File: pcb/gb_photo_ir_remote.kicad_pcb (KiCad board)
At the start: 2 copper layers, 28 x 41 mm, 10 parts, among them SW1 SW_Push_SPDT, SW2 SW_Push_SPDT, U1 NE555P

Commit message: build
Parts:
- added M1: MountingHole_2.5mm, MountingHole:MountingHole_2.5mm, F.Cu at (123.0, 31.0)
- added M2: MountingHole_2.5mm, MountingHole:MountingHole_2.5mm, F.Cu at (152.0, 31.0)
- added M3: MountingHole_2.5mm, MountingHole:MountingHole_2.5mm, F.Cu at (123.0, 80.0)
- BT1: footprint Battery:BatteryHolder_Keystone_1060_1x2032 -> REB:REB_BatteryHolder_2032
- C1: footprint Capacitor_THT:C_Disc_D5.1mm_W3.2mm_P5.00mm -> Capacitor_THT:C_Disc_D5.0mm_W2.5mm_P2.50mm
- D1, D2: footprint LED_THT:LED_D5.0mm_Horizontal_O3.81mm_Z3.0mm -> LED_THT:LED_D5.0mm_Horizontal_O1.27mm_Z3.0mm
- moved U1 41.8 mm to (128.5, 79.8), turned to 90 degrees
- moved C1 40.1 mm to (146.8, 77.8), turned to 45 degrees
- moved R2 19.2 mm to (147.6, 70.3), turned to -135 degrees
- moved R1 18.0 mm to (150.7, 37.6), turned to 180 degrees
- moved R3 8.30 mm to (135.8, 37.6), turned to 180 degrees
- moved SW2 8.23 mm to (124.2, 63.1)
- moved SW1 7.20 mm to (144.7, 62.2)
- moved D1 5.98 mm to (144.3, 33.0)
- moved D2 4.45 mm to (134.2, 33.1)
- moved BT1 1.24 mm to (136.8, 50.7), turned to 0 degrees
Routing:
- net /OUT: track 0.00 -> 51.1 mm
- net Net-(D2-A): track 0.00 -> 49.4 mm
- net +BATT: track 0.00 -> 39.9 mm
- net /VIN: track 0.00 -> 39.7 mm
- net /DIS: track 0.00 -> 25.7 mm
- net Net-(D1-K): track 0.00 -> 9.38 mm
- net Net-(D2-K): track 0.00 -> 5.16 mm
- net GND: vias 0 -> 16
- added copper zone on B.Cu, net GND
- added copper zone on F.Cu, net GND
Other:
- board size 28 x 41 mm -> 35 x 55 mm

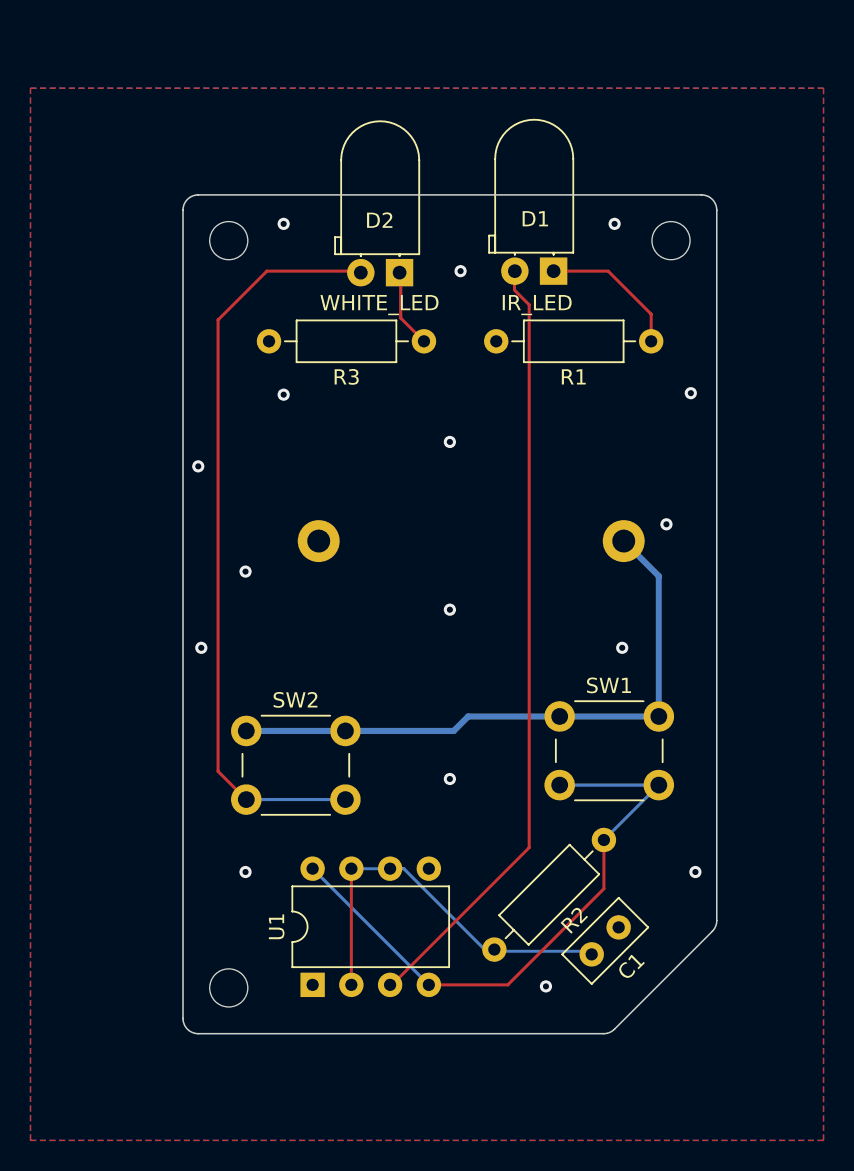
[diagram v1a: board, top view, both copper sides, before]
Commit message: Timer didn't use an actual divider?
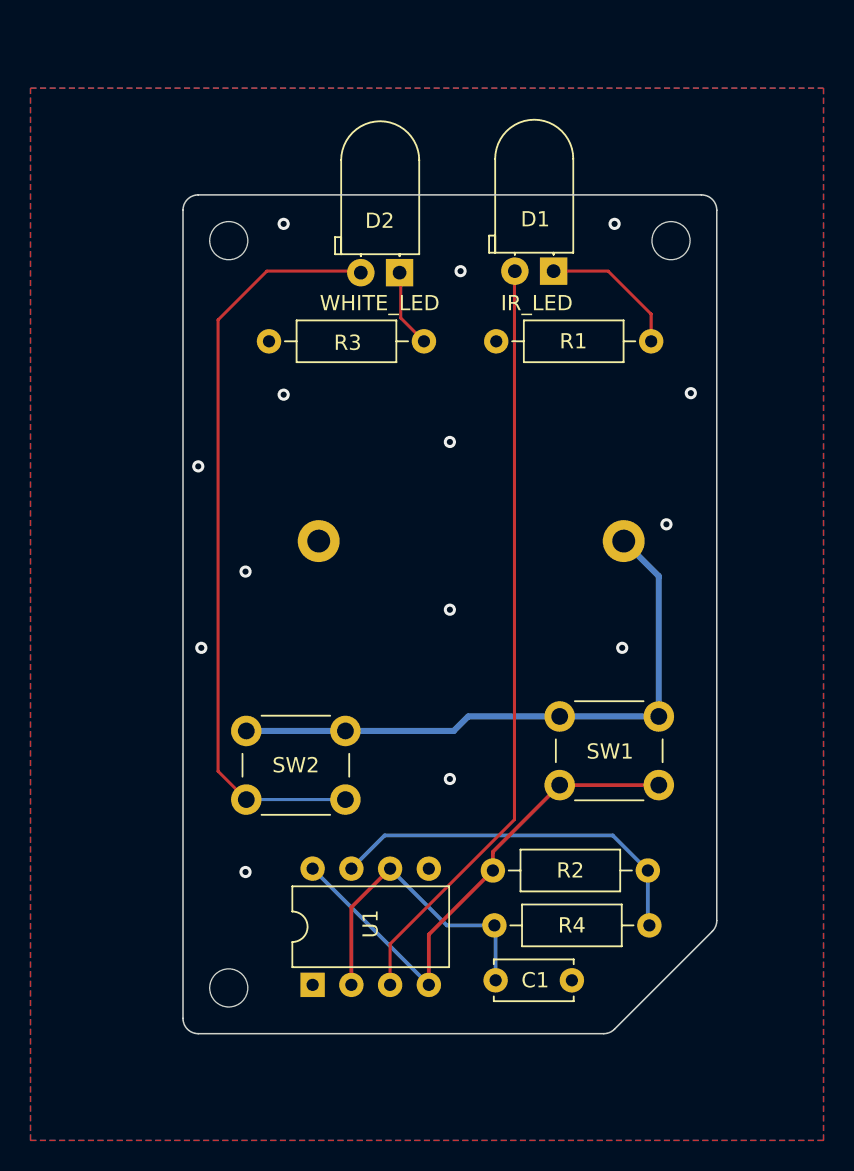
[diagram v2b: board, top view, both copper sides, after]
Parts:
- added R4: 1M, Resistor_THT:R_Axial_DIN0207_L6.3mm_D2.5mm_P10.16mm_Horizontal, F.Cu at (150.6, 75.9)
- C1: value 0.1u -> 4.7n; footprint Capacitor_THT:C_Disc_D5.0mm_W2.5mm_P2.50mm -> Capacitor_THT:C_Disc_D5.0mm_W2.5mm_P5.00mm
- R1, R3: value 75R -> 47R
- R2: value 100K -> 1M
- moved C1 6.53 mm to (140.5, 79.5), turned to 0 degrees
- moved R2 3.51 mm to (150.5, 72.3), turned to 180 degrees
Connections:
- net /OUT renamed /5_OUT
- C1 pad 1: /DIS -> /5_SINK
- R2 pad 1: /VIN -> /5_DIV
- R2 pad 2: /DIS -> /VIN
- U1 pad 2: /DIS -> /5_SINK
- U1 pad 6: /DIS -> /5_SINK
- U1 pad 7: /DIS -> /5_DIV
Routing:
- net /DIS: track 25.7 -> 0.00 mm
- net /5_DIV: track 0.00 -> 24.9 mm
- net /5_SINK: track 0.00 -> 20.7 mm
- net /VIN: track 39.7 -> 33.9 mm
- net /5_OUT: track 51.1 -> 50.3 mm
- net GND: vias 16 -> 14
